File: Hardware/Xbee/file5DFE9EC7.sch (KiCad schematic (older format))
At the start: 10 parts, among them Q3 DMP3099L-7, U1 AZ1117-3.3

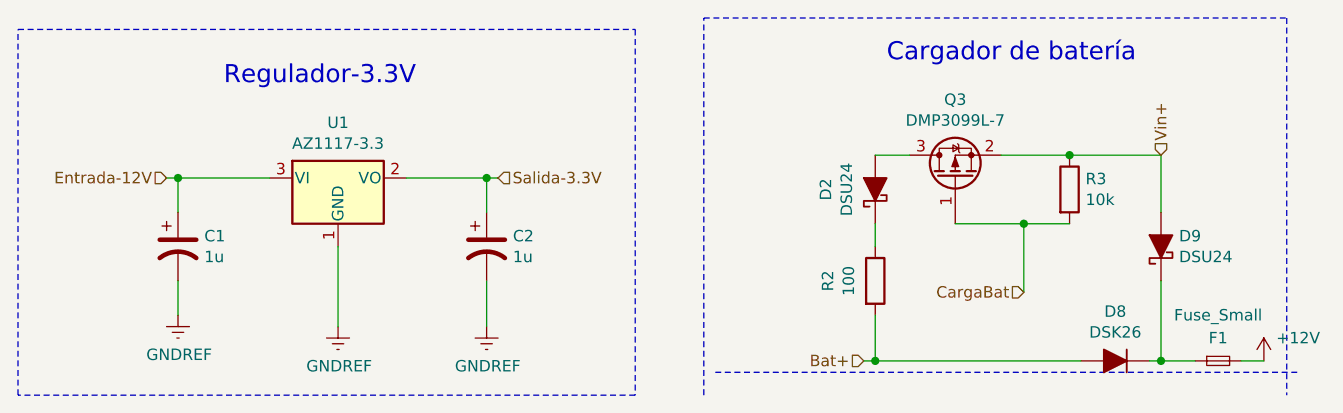
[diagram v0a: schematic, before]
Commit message: Change footprints 2
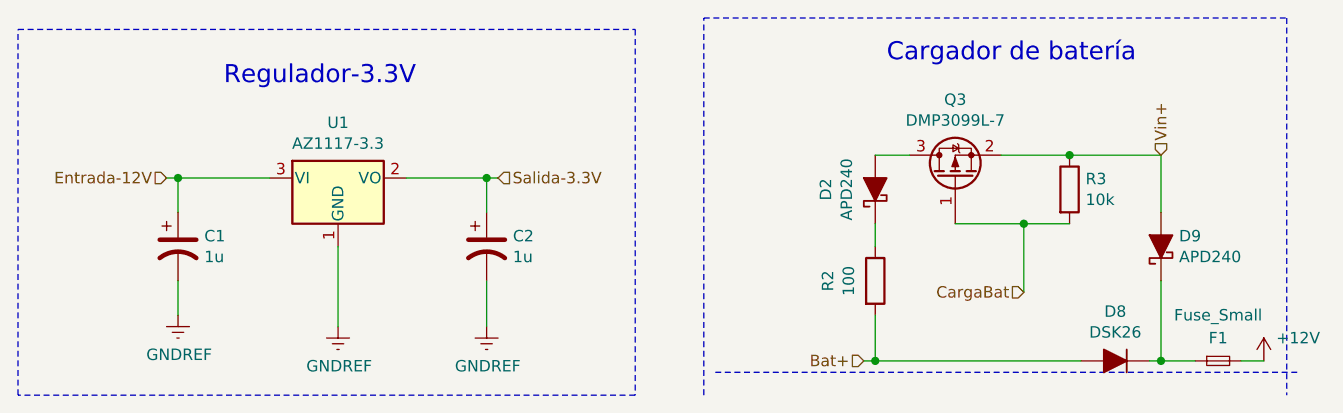
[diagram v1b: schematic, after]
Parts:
- D2, D9: value DSU24 -> APD240; Código Proveedor 1 (none) -> APD240KDTR-G1DITR-ND; Link Proveedor 1 (none) -> https://www.digikey.com/product-detail/es/diodes-incorporat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; Nombre Fabricante (none) -> APD240KDTR-G1; Package (none) -> SOD-123
- Q3: Código Proveedor 1 (none) -> DMP3099L-7DITR-ND; Link Proveedor 1 (none) -> https://www.digikey.com/product-detail/en/diodes-incorporat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; Nombre Fabricante (none) -> DMP3099L-7; Package (none) -> SOT-23
- R2: Código Proveedor 1 (none) -> 311-100FRTR-ND; Link Proveedor 1 (none) -> https://www.digikey.com/product-detail/es/yageo/RC1206FR-07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; Nombre Fabricante (none) -> RC1206FR-07100RL; Package (none) -> 1206
- R3: footprint Resistor_SMD:R_0805_2012Metric_Pad1.15x1.40mm_HandSolder -> Resistor_SMD:R_1206_3216Metric_Pad1.42x1.75mm_HandSolder; Código Proveedor 1 (none) -> 311-10KERCT-ND; Link Proveedor 1 (none) -> https://www.digikey.com/product-detail/en/yageo/RC1206JR-07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; Nombre Fabricante (none) -> RC1206JR-0710KL; Package (none) -> 1206
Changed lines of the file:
@@
 EESchema Schematic File Version 4
 LIBS:Xbee-cache
-EELAYER 30 0
+EELAYER 29 0
 EELAYER END
 $Descr A4 11693 8268
@@
 P 4600 1600
 F 0 "D2" H 4600 1816 50  0000 C CNN
-F 1 "DSU24" H 4600 1725 50  0000 C CNN
+F 1 "APD240" H 4600 1725 50  0000 C CNN
 F 2 "Diode_SMD:D_SOD-123" H 4600 1600 50  0001 C CNN
 F 3 "~" H 4600 1600 50  0001 C CNN
+F 4 "APD240KDTR-G1" H 4600 1600 50  0001 C CNN "Nombre Fabricante"
+F 5 "APD240KDTR-G1DITR-ND" H 4600 1600 50  0001 C CNN "Código Proveedor 1"
+F 6 "https://www.digikey.com/product-detail/es/diodes-incorporated/APD240KDTR-G1/APD240KDTR-G1DITR-ND/5721492" H 4600 1600 50  0001 C CNN "Link Proveedor 1"
+F 7 "SOD-123" H 4600 1600 50  0001 C CNN "Package"
 	1    4600 1600
 	0    -1   -1   0
@@
 F 0 "R3" H 5520 1646 50  0000 L CNN
 F 1 "10k" H 5520 1555 50  0000 L CNN
-F 2 "Resistor_SMD:R_0805_2012Metric_Pad1.15x1.40mm_HandSolder" V 5380 1600 50  0001 C CNN
+F 2 "Resistor_SMD:R_1206_3216Metric_Pad1.42x1.75mm_HandSolder" V 5380 1600 50  0001 C CNN
 F 3 "~" H 5450 1600 50  0001 C CNN
+F 4 "RC1206JR-0710KL" H 5450 1600 50  0001 C CNN "Nombre Fabricante"
+F 5 "1206" H 5450 1600 50  0001 C CNN "Package"
+F 6 "311-10KERCT-ND" H 5450 1600 50  0001 C CNN "Código Proveedor 1"
+F 7 "https://www.digikey.com/product-detail/en/yageo/RC1206JR-0710KL/311-10KERCT-ND/732156" H 5450 1600 50  0001 C CNN "Link Proveedor 1"
 	1    5450 1600
 	1    0    0    -1
@@
 P 5850 1850
 F 0 "D9" V 5896 1771 50  0000 R CNN
-F 1 "DSU24" V 5805 1771 50  0000 R CNN
+F 1 "APD240" V 5805 1771 50  0000 R CNN
 F 2 "Diode_SMD:D_SOD-123" H 5850 1850 50  0001 C CNN
 F 3 "~" H 5850 1850 50  0001 C CNN
+F 4 " 	APD240KDTR-G1" H 5850 1850 50  0001 C CNN "Nombre Fabricante"
+F 5 "APD240KDTR-G1DITR-ND" H 5850 1850 50  0001 C CNN "Código Proveedor 1"
+F 6 "https://www.digikey.com/product-detail/es/diodes-incorporated/APD240KDTR-G1/APD240KDTR-G1DITR-ND/5721492" H 5850 1850 50  0001 C CNN "Link Proveedor 1"
+F 7 "SOD-123" H 5850 1850 50  0001 C CNN "Package"
 	1    5850 1850
 	0    -1   -1   0
@@
 F 2 "Resistor_SMD:R_1218_3246Metric_Pad1.22x4.75mm_HandSolder" V 4530 2000 50  0001 C CNN
 F 3 "~" H 4600 2000 50  0001 C CNN
+F 4 "https://www.digikey.com/product-detail/es/yageo/RC1206FR-07100RL/311-100FRTR-ND/728491" H 4600 2000 50  0001 C CNN "Link Proveedor 1"
+F 5 "1206" H 4600 2000 50  0001 C CNN "Package"
+F 6 "311-100FRTR-ND " H 4600 2000 50  0001 C CNN "Código Proveedor 1"
+F 7 "RC1206FR-07100RL" H 4600 2000 50  0001 C CNN "Nombre Fabricante"
 	1    4600 2000
 	1    0    0    -1
@@
 F 2 "Package_TO_SOT_SMD:SOT-23" H 5150 1650 50  0001 C CNN
 F 3 "~" H 4950 1550 50  0001 C CNN
+F 4 "DMP3099L-7" H 4950 1550 50  0001 C CNN "Nombre Fabricante"
+F 5 "DMP3099L-7DITR-ND" H 4950 1550 50  0001 C CNN "Código Proveedor 1"
+F 6 "https://www.digikey.com/product-detail/en/diodes-incorporated/DMP3099L-7/DMP3099L-7DITR-ND/4471075" H 4950 1550 50  0001 C CNN "Link Proveedor 1"
+F 7 "SOT-23" H 4950 1550 50  0001 C CNN "Package"
 	1    4950 1550
 	0    -1   -1   0

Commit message: Footprints 3
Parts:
- C1, C2: footprint Capacitor_SMD:C_0805_2012Metric_Pad1.15x1.40mm_HandSolder -> Capacitor_SMD:C_1206_3216Metric_Pad1.42x1.75mm_HandSolder; Código Proveedor 1 (none) -> 399-8150-1-ND; Link Proveedor 1 (none) -> https://www.digikey.com/product-detail/en/kemet/C1206C105M4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; Nombre Fabricante (none) -> C1206C105M4RACTU; Package (none) -> 1206
- D2, D9: Código Proveedor 1 APD240KDTR-G1DITR-ND -> APD240KDTR-G1DICT-ND; Link Proveedor 1 https://www.digikey.com/product-detail/es/diodes-incorporated/APD240KDTR-G1/APD240KDTR-G1DITR-ND/5721492 -> https://www.digikey.com/product-detail/es/diodes-incorporated/APD240KDTR-G1/APD240KDTR-G1DICT-ND/7708824
- D8: value DSK26 -> MURA220; footprint Diode_SMD:D_SOD-123F -> Diode_SMD:D_SMA; Código Proveedor 1 (none) -> MURA220T3GOSCT-ND; Link Proveedor 1 (none) -> https://www.digikey.com/product-detail/en/on-semiconductor/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; Nombre Fabricante (none) -> MURA220T3G; Package (none) -> SMA
- F1: Código Proveedor 1 (none) -> 507-1881-1-ND; Link Proveedor 1 (none) -> https://www.digikey.com/product-detail/en/bel-fuse-inc/C1F-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; Nombre Fabricante (none) -> C1F 2; Package (none) -> 1206
- Q3: Código Proveedor 1 DMP3099L-7DITR-ND -> DMP3099L-7DICT-ND; Link Proveedor 1 https://www.digikey.com/product-detail/en/diodes-incorporated/DMP3099L-7/DMP3099L-7DITR-ND/4471075 -> https://www.digikey.com/product-detail/en/diodes-incorporated/DMP3099L-7/DMP3099L-7DICT-ND/5218217
- U1: Código Proveedor 1 (none) -> AZ1117EH-3.3TRG1DICT-ND; Link Proveedor 1 (none) -> https://www.digikey.com/product-detail/en/diodes-incorporat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; Nombre Fabricante (none) -> Diodes Incorporated; Package (none) -> SOT-223
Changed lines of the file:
@@
 EESchema Schematic File Version 4
 LIBS:Xbee-cache
-EELAYER 29 0
+EELAYER 30 0
 EELAYER END
 $Descr A4 11693 8268
@@
 F 0 "C1" H 1665 1896 50  0000 L CNN
 F 1 "1u" H 1665 1805 50  0000 L CNN
-F 2 "Capacitor_SMD:C_0805_2012Metric_Pad1.15x1.40mm_HandSolder" H 1550 1850 50  0001 C CNN
+F 2 "Capacitor_SMD:C_1206_3216Metric_Pad1.42x1.75mm_HandSolder" H 1550 1850 50  0001 C CNN
 F 3 "~" H 1550 1850 50  0001 C CNN
+F 4 "C1206C105M4RACTU" H 1550 1850 50  0001 C CNN "Nombre Fabricante"
+F 5 "399-8150-1-ND" H 1550 1850 50  0001 C CNN "Código Proveedor 1"
+F 6 "https://www.digikey.com/product-detail/en/kemet/C1206C105M4RACTU/399-8150-1-ND/3471873" H 1550 1850 50  0001 C CNN "Link Proveedor 1"
+F 7 "1206" H 1550 1850 50  0001 C CNN "Package"
 	1    1550 1850
 	1    0    0    -1
@@
 F 0 "C2" H 3015 1896 50  0000 L CNN
 F 1 "1u" H 3015 1805 50  0000 L CNN
-F 2 "Capacitor_SMD:C_0805_2012Metric_Pad1.15x1.40mm_HandSolder" H 2900 1850 50  0001 C CNN
+F 2 "Capacitor_SMD:C_1206_3216Metric_Pad1.42x1.75mm_HandSolder" H 2900 1850 50  0001 C CNN
 F 3 "~" H 2900 1850 50  0001 C CNN
+F 4 "C1206C105M4RACTU" H 2900 1850 50  0001 C CNN "Nombre Fabricante"
+F 5 "399-8150-1-ND" H 2900 1850 50  0001 C CNN "Código Proveedor 1"
+F 6 "https://www.digikey.com/product-detail/en/kemet/C1206C105M4RACTU/399-8150-1-ND/3471873" H 2900 1850 50  0001 C CNN "Link Proveedor 1"
+F 7 "1206" H 2900 1850 50  0001 C CNN "Package"
 	1    2900 1850
 	1    0    0    -1
@@
 F 2 "Package_TO_SOT_SMD:SOT-223-3_TabPin2" H 2250 1800 50  0001 C CIN
 F 3 "https://www.diodes.com/assets/Datasheets/AZ1117.pdf" H 2250 1550 50  0001 C CNN
+F 4 "Diodes Incorporated" H 2250 1550 50  0001 C CNN "Nombre Fabricante"
+F 5 "AZ1117EH-3.3TRG1DICT-ND" H 2250 1550 50  0001 C CNN "Código Proveedor 1"
+F 6 "https://www.digikey.com/product-detail/en/diodes-incorporated/AZ1117EH-3.3TRG1/AZ1117EH-3.3TRG1DICT-ND/5001336" H 2250 1550 50  0001 C CNN "Link Proveedor 1"
+F 7 "SOT-223" H 2250 1550 50  0001 C CNN "Package"
 	1    2250 1550
 	1    0    0    -1
@@
 F 3 "~" H 4600 1600 50  0001 C CNN
 F 4 "APD240KDTR-G1" H 4600 1600 50  0001 C CNN "Nombre Fabricante"
-F 5 "APD240KDTR-G1DITR-ND" H 4600 1600 50  0001 C CNN "Código Proveedor 1"
-F 6 "https://www.digikey.com/product-detail/es/diodes-incorporated/APD240KDTR-G1/APD240KDTR-G1DITR-ND/5721492" H 4600 1600 50  0001 C CNN "Link Proveedor 1"
+F 5 "APD240KDTR-G1DICT-ND" H 4600 1600 50  0001 C CNN "Código Proveedor 1"
+F 6 "https://www.digikey.com/product-detail/es/diodes-incorporated/APD240KDTR-G1/APD240KDTR-G1DICT-ND/7708824" H 4600 1600 50  0001 C CNN "Link Proveedor 1"
 F 7 "SOD-123" H 4600 1600 50  0001 C CNN "Package"
 	1    4600 1600
@@
 P 5650 2350
 F 0 "D8" H 5650 2134 50  0000 C CNN
-F 1 "DSK26" H 5650 2225 50  0000 C CNN
-F 2 "Diode_SMD:D_SOD-123F" H 5650 2350 50  0001 C CNN
+F 1 "MURA220" H 5650 2225 50  0000 C CNN
+F 2 "Diode_SMD:D_SMA" H 5650 2350 50  0001 C CNN
 F 3 "~" H 5650 2350 50  0001 C CNN
+F 4 "MURA220T3G" H 5650 2350 50  0001 C CNN "Nombre Fabricante"
+F 5 "MURA220T3GOSCT-ND" H 5650 2350 50  0001 C CNN "Código Proveedor 1"
+F 6 "https://www.digikey.com/product-detail/en/on-semiconductor/MURA220T3G/MURA220T3GOSCT-ND/921212" H 5650 2350 50  0001 C CNN "Link Proveedor 1"
+F 7 "SMA" H 5650 2350 50  0001 C CNN "Package"
 	1    5650 2350
 	-1   0    0    1
@@
 F 3 "~" H 5850 1850 50  0001 C CNN
 F 4 " 	APD240KDTR-G1" H 5850 1850 50  0001 C CNN "Nombre Fabricante"
-F 5 "APD240KDTR-G1DITR-ND" H 5850 1850 50  0001 C CNN "Código Proveedor 1"
-F 6 "https://www.digikey.com/product-detail/es/diodes-incorporated/APD240KDTR-G1/APD240KDTR-G1DITR-ND/5721492" H 5850 1850 50  0001 C CNN "Link Proveedor 1"
+F 5 "APD240KDTR-G1DICT-ND" H 5850 1850 50  0001 C CNN "Código Proveedor 1"
+F 6 "https://www.digikey.com/product-detail/es/diodes-incorporated/APD240KDTR-G1/APD240KDTR-G1DICT-ND/7708824" H 5850 1850 50  0001 C CNN "Link Proveedor 1"
 F 7 "SOD-123" H 5850 1850 50  0001 C CNN "Package"
 	1    5850 1850
@@
 F 3 "~" H 4950 1550 50  0001 C CNN
 F 4 "DMP3099L-7" H 4950 1550 50  0001 C CNN "Nombre Fabricante"
-F 5 "DMP3099L-7DITR-ND" H 4950 1550 50  0001 C CNN "Código Proveedor 1"
-F 6 "https://www.digikey.com/product-detail/en/diodes-incorporated/DMP3099L-7/DMP3099L-7DITR-ND/4471075" H 4950 1550 50  0001 C CNN "Link Proveedor 1"
+F 5 "DMP3099L-7DICT-ND" H 4950 1550 50  0001 C CNN "Código Proveedor 1"
+F 6 "https://www.digikey.com/product-detail/en/diodes-incorporated/DMP3099L-7/DMP3099L-7DICT-ND/5218217" H 4950 1550 50  0001 C CNN "Link Proveedor 1"
 F 7 "SOT-23" H 4950 1550 50  0001 C CNN "Package"
 	1    4950 1550
@@
 F 2 "Fuse:Fuse_1206_3216Metric_Pad1.42x1.75mm_HandSolder" H 6100 2350 50  0001 C CNN
 F 3 "~" H 6100 2350 50  0001 C CNN
+F 4 "C1F 2" H 6100 2350 50  0001 C CNN "Nombre Fabricante"
+F 5 "507-1881-1-ND" H 6100 2350 50  0001 C CNN "Código Proveedor 1"
+F 6 "https://www.digikey.com/product-detail/en/bel-fuse-inc/C1F-2/507-1881-1-ND/4968159" H 6100 2350 50  0001 C CNN "Link Proveedor 1"
+F 7 "1206" H 6100 2350 50  0001 C CNN "Package"
 	1    6100 2350
 	1    0    0    -1
